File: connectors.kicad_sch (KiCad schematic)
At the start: 12 parts, among them J1101 VN_1611_Interface, J1102 AMPSEAL_35, J1103 Banana_Jack, J1104 Banana_Jack

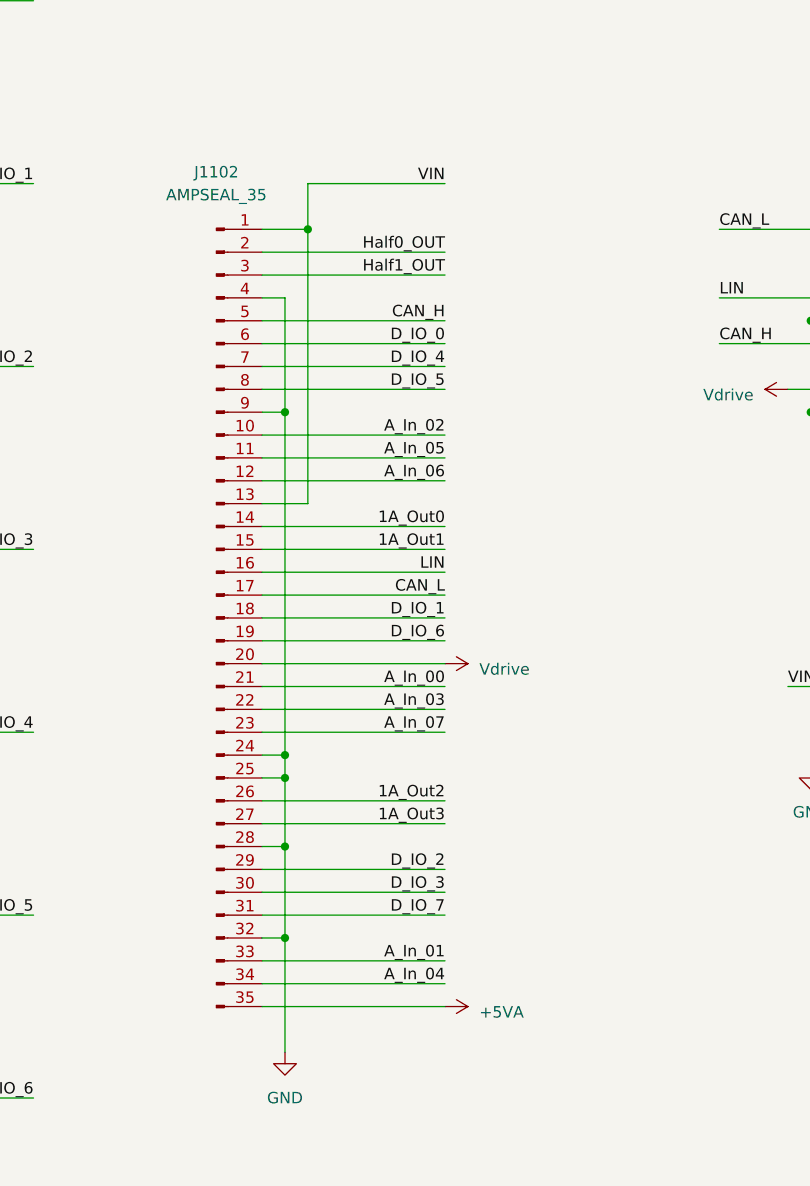
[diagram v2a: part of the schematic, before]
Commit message: placed components and began routing
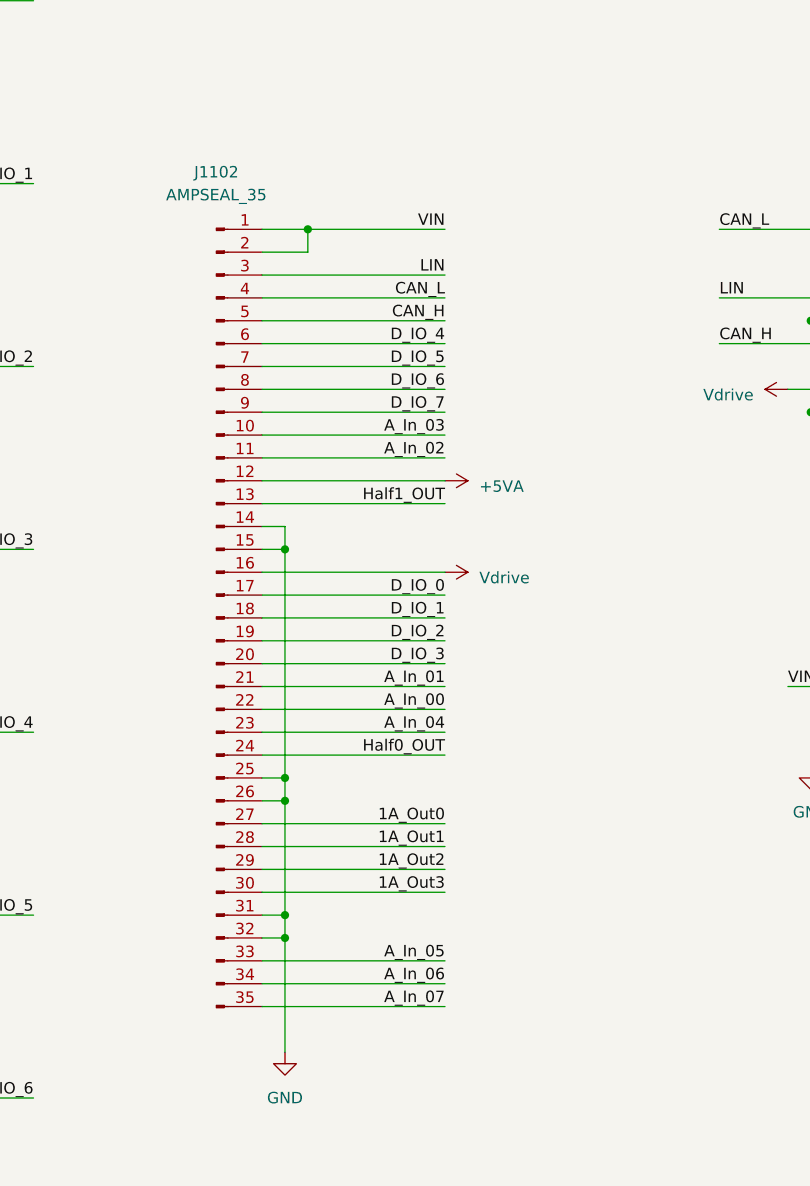
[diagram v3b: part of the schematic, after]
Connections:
- net +5VA: now also J1102.12 (Pin_12); no longer J1102.35 (Pin_35)
- net 1A_Out0: now also J1102.27 (Pin_27); no longer J1102.14 (Pin_14)
- net 1A_Out1: now also J1102.28 (Pin_28); no longer J1102.15 (Pin_15)
- net 1A_Out2: now also J1102.29 (Pin_29); no longer J1102.26 (Pin_26)
- net 1A_Out3: now also J1102.30 (Pin_30); no longer J1102.27 (Pin_27)
- net A_In_00: now also J1102.22 (Pin_22); no longer J1102.21 (Pin_21)
- net A_In_01: now also J1102.21 (Pin_21); no longer J1102.33 (Pin_33)
- net A_In_02: now also J1102.11 (Pin_11); no longer J1102.10 (Pin_10)
- net A_In_03: now also J1102.10 (Pin_10); no longer J1102.22 (Pin_22)
- net A_In_04: now also J1102.23 (Pin_23); no longer J1102.34 (Pin_34)
- net A_In_05: now also J1102.33 (Pin_33); no longer J1102.11 (Pin_11)
- net A_In_06: now also J1102.34 (Pin_34); no longer J1102.12 (Pin_12)
- net A_In_07: now also J1102.35 (Pin_35); no longer J1102.23 (Pin_23)
- net CAN_L: now also J1102.4 (Pin_4); no longer J1102.17 (Pin_17)
- net D_IO_0: now also J1102.17 (Pin_17); no longer J1102.6 (Pin_6)
- net D_IO_2: now also J1102.19 (Pin_19); no longer J1102.29 (Pin_29)
- net D_IO_3: now also J1102.20 (Pin_20); no longer J1102.30 (Pin_30)
- net D_IO_4: now also J1102.6 (Pin_6); no longer J1102.7 (Pin_7)
- net D_IO_5: now also J1102.7 (Pin_7); no longer J1102.8 (Pin_8)
- net D_IO_6: now also J1102.8 (Pin_8); no longer J1102.19 (Pin_19)
- net D_IO_7: now also J1102.9 (Pin_9); no longer J1102.31 (Pin_31)
- net GND: now also J1102.14 (Pin_14), J1102.15 (Pin_15), J1102.26 (Pin_26), J1102.31 (Pin_31); no longer J1102.24 (Pin_24), J1102.28 (Pin_28), J1102.4 (Pin_4), J1102.9 (Pin_9)
- net Half0_OUT: now also J1102.24 (Pin_24); no longer J1102.2 (Pin_2)
- net Half1_OUT: now also J1102.13 (Pin_13); no longer J1102.3 (Pin_3)
- net LIN: now also J1102.3 (Pin_3); no longer J1102.16 (Pin_16)
- net VIN: now also J1102.2 (Pin_2); no longer J1102.13 (Pin_13)
- net Vdrive: now also J1102.16 (Pin_16); no longer J1102.20 (Pin_20)

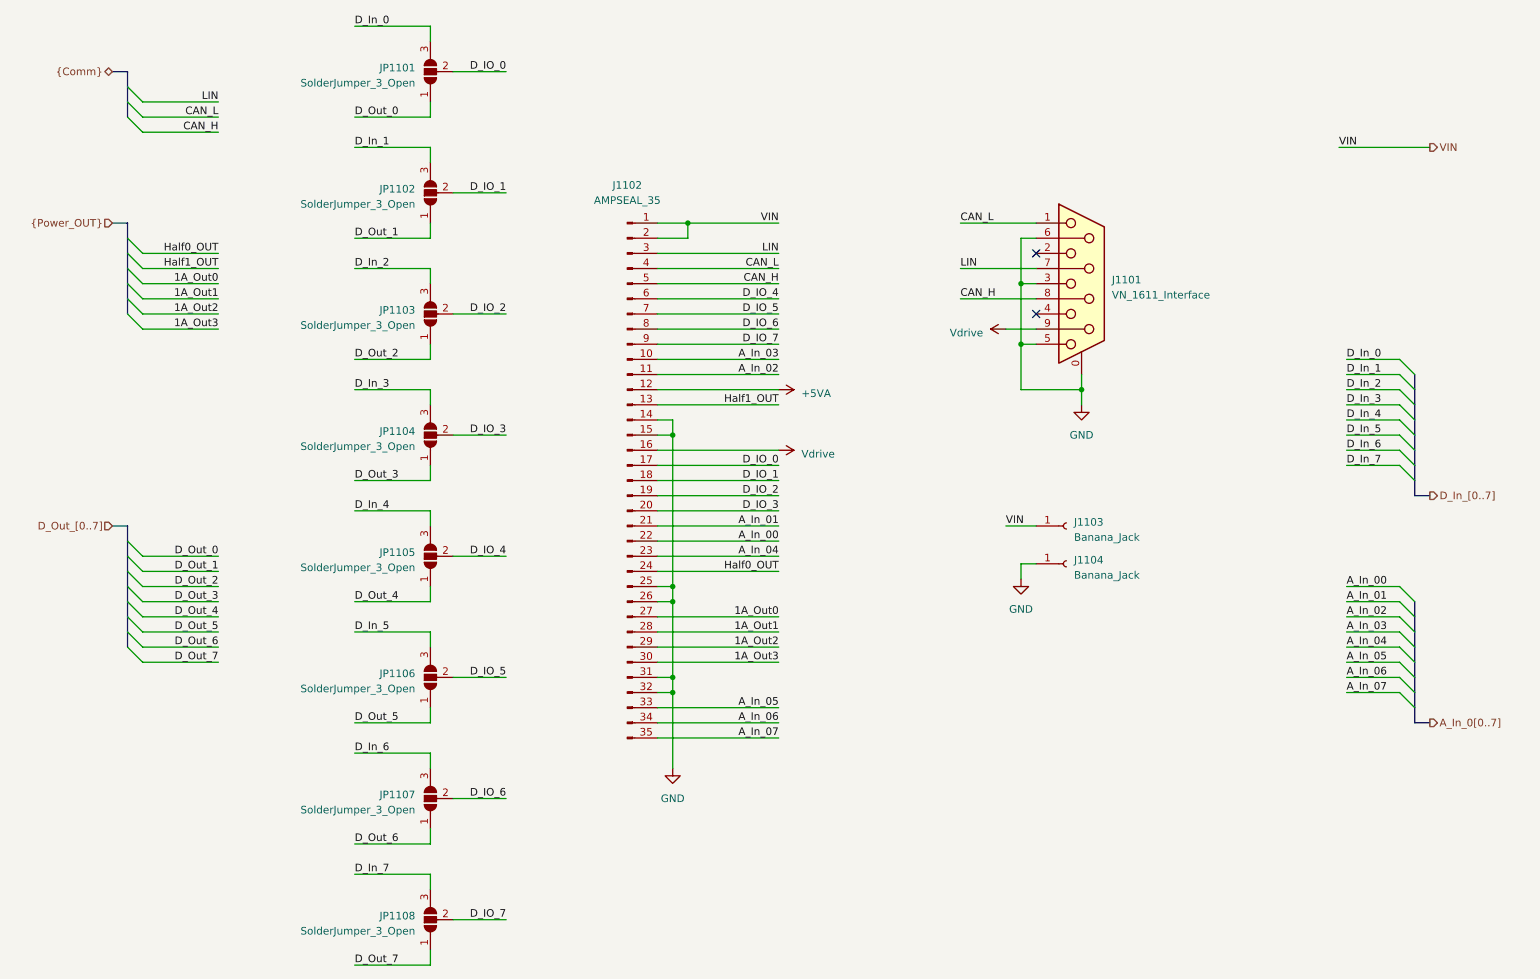
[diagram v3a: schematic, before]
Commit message: hierarchical sheets for digital I/O and replaced power supply jumpers with relays
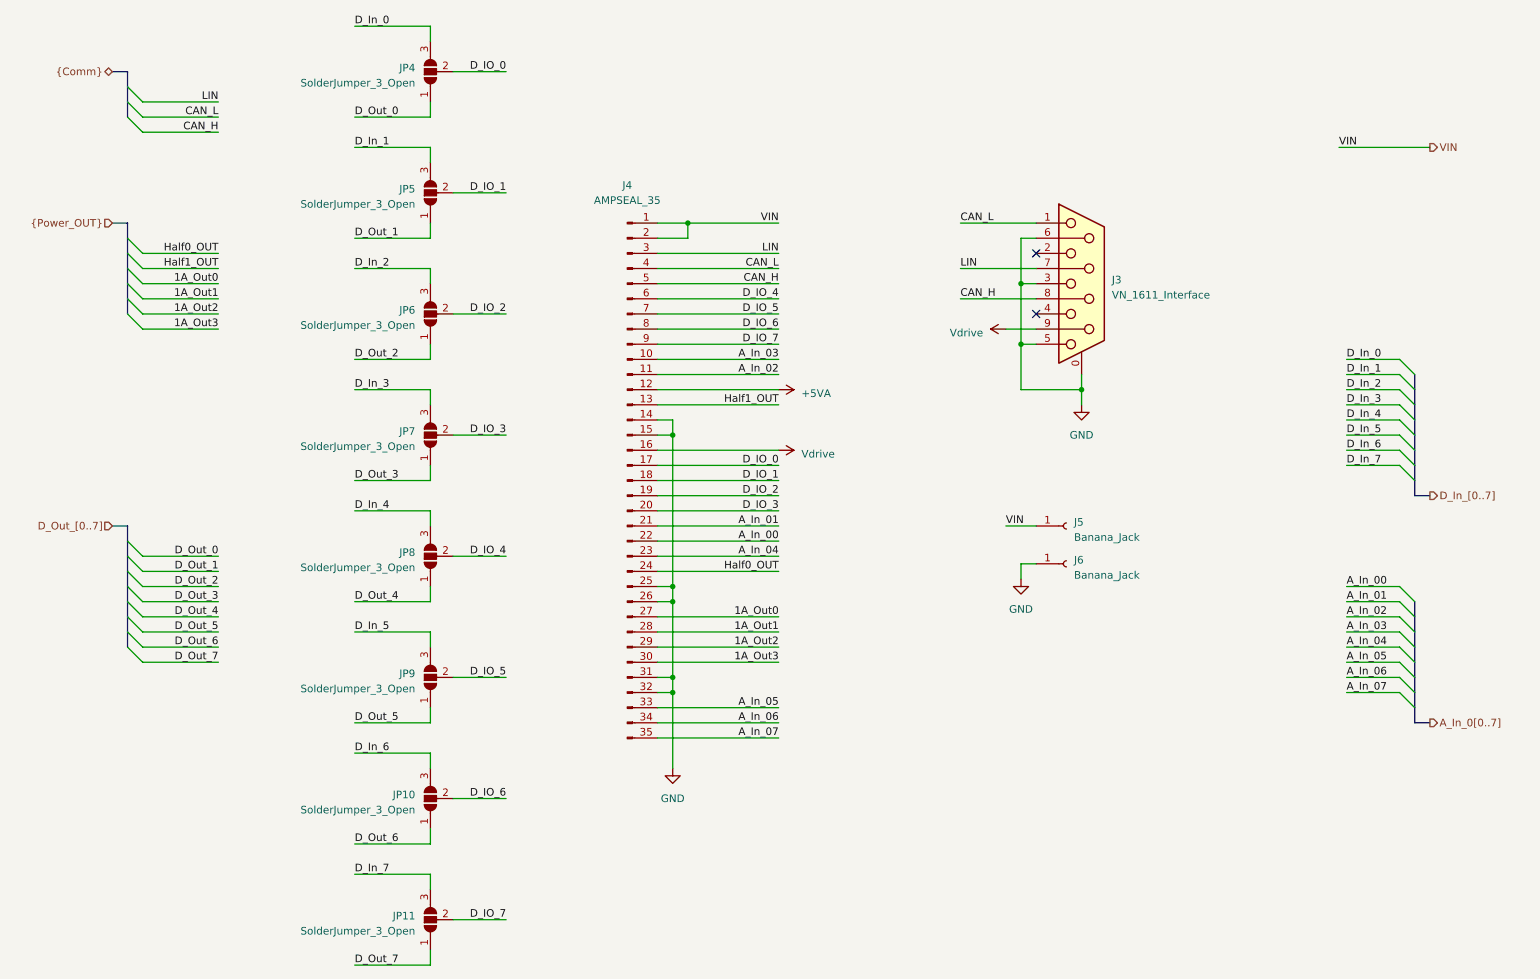
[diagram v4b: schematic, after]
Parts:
- renumbered J1101 to J3, J1102 to J4, J1103 to J5, J1104 to J6, JP1107 to JP10, JP1108 to JP11, JP1101 to JP4, JP1102 to JP5, JP1103 to JP6, JP1104 to JP7, JP1105 to JP8, JP1106 to JP9
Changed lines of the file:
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@@
   (symbol (lib_id "Jumper:SolderJumper_3_Open") (at 88.9 127 90) (unit 1)
     (in_bom yes) (on_board yes) (dnp no) (fields_autoplaced)
-    (property "Reference" "JP1106" (at 86.36 126.365 90)
+    (property "Reference" "JP9" (at 86.36 126.365 90)
       (effects (font (size 1.27 1.27)) (justify left))
     )
@@
       (project "Sensor_Board"
         (path "/e2a0eb17-0eae-4cdd-befd-118f8728b921/276bb215-b19a-4afa-b073-6f1d222ea979"
-          (reference "JP1106") (unit 1)
+          (reference "JP9") (unit 1)
         )
       )
@@
   (symbol (lib_id "power:Vdrive") (at 147.32 88.9 270) (unit 1)
     (in_bom yes) (on_board yes) (dnp no) (fields_autoplaced)
-    (property "Reference" "#PWR01103" (at 143.51 83.82 0)
+    (property "Reference" "#PWR0148" (at 143.51 83.82 0)
       (effects (font (size 1.27 1.27)) hide)
     )
@@
       (project "Sensor_Board"
         (path "/e2a0eb17-0eae-4cdd-befd-118f8728b921/276bb215-b19a-4afa-b073-6f1d222ea979"
-          (reference "#PWR01103") (unit 1)
+          (reference "#PWR0148") (unit 1)
         )
       )
@@
   (symbol (lib_id "power:GND") (at 198.12 81.28 0) (unit 1)
     (in_bom yes) (on_board yes) (dnp no) (fields_autoplaced)
-    (property "Reference" "#PWR01102" (at 198.12 87.63 0)
+    (property "Reference" "#PWR0147" (at 198.12 87.63 0)
       (effects (font (size 1.27 1.27)) hide)
     )
@@
       (project "Sensor_Board"
         (path "/e2a0eb17-0eae-4cdd-befd-118f8728b921/276bb215-b19a-4afa-b073-6f1d222ea979"
-          (reference "#PWR01102") (unit 1)
+          (reference "#PWR0147") (unit 1)
         )
       )
@@
   (symbol (lib_id "Connector:DE9_Receptacle_MountingHoles") (at 198.12 60.96 0) (unit 1)
     (in_bom yes) (on_board yes) (dnp no) (fields_autoplaced)
-    (property "Reference" "J1101" (at 203.2 60.325 0)
+    (property "Reference" "J3" (at 203.2 60.325 0)
       (effects (font (size 1.27 1.27)) (justify left))
     )
@@
       (project "Sensor_Board"
         (path "/e2a0eb17-0eae-4cdd-befd-118f8728b921/276bb215-b19a-4afa-b073-6f1d222ea979"
-          (reference "J1101") (unit 1)
+          (reference "J3") (unit 1)
         )
       )
@@
   (symbol (lib_id "Connector:Conn_01x01_Socket") (at 195.58 101.6 0) (unit 1)
     (in_bom yes) (on_board yes) (dnp no) (fields_autoplaced)
-    (property "Reference" "J1103" (at 196.85 100.965 0)
+    (property "Reference" "J5" (at 196.85 100.965 0)
       (effects (font (size 1.27 1.27)) (justify left))
     )
@@
       (project "Sensor_Board"
         (path "/e2a0eb17-0eae-4cdd-befd-118f8728b921/276bb215-b19a-4afa-b073-6f1d222ea979"
-          (reference "J1103") (unit 1)
+          (reference "J5") (unit 1)
         )
       )
@@
   (symbol (lib_id "Jumper:SolderJumper_3_Open") (at 88.9 25.4 90) (unit 1)
     (in_bom yes) (on_board yes) (dnp no) (fields_autoplaced)
-    (property "Reference" "JP1101" (at 86.36 24.765 90)
+    (property "Reference" "JP4" (at 86.36 24.765 90)
       (effects (font (size 1.27 1.27)) (justify left))
     )
@@
       (project "Sensor_Board"
         (path "/e2a0eb17-0eae-4cdd-befd-118f8728b921/276bb215-b19a-4afa-b073-6f1d222ea979"
-          (reference "JP1101") (unit 1)
+          (reference "JP4") (unit 1)
         )
       )
@@
   (symbol (lib_id "power:GND") (at 187.96 110.49 0) (unit 1)
     (in_bom yes) (on_board yes) (dnp no) (fields_autoplaced)
-    (property "Reference" "#PWR01104" (at 187.96 116.84 0)
+    (property "Reference" "#PWR0149" (at 187.96 116.84 0)
       (effects (font (size 1.27 1.27)) hide)
     )
@@
       (project "Sensor_Board"
         (path "/e2a0eb17-0eae-4cdd-befd-118f8728b921/276bb215-b19a-4afa-b073-6f1d222ea979"
-          (reference "#PWR01104") (unit 1)
+          (reference "#PWR0149") (unit 1)
         )
       )
@@
   (symbol (lib_id "Jumper:SolderJumper_3_Open") (at 88.9 106.68 90) (unit 1)
     (in_bom yes) (on_board yes) (dnp no) (fields_autoplaced)
-    (property "Reference" "JP1105" (at 86.36 106.045 90)
+    (property "Reference" "JP8" (at 86.36 106.045 90)
       (effects (font (size 1.27 1.27)) (justify left))
     )
@@
       (project "Sensor_Board"
         (path "/e2a0eb17-0eae-4cdd-befd-118f8728b921/276bb215-b19a-4afa-b073-6f1d222ea979"
-          (reference "JP1105") (unit 1)
+          (reference "JP8") (unit 1)
         )
       )
@@
   (symbol (lib_id "Jumper:SolderJumper_3_Open") (at 88.9 147.32 90) (unit 1)
     (in_bom yes) (on_board yes) (dnp no) (fields_autoplaced)
-    (property "Reference" "JP1107" (at 86.36 146.685 90)
+    (property "Reference" "JP10" (at 86.36 146.685 90)
       (effects (font (size 1.27 1.27)) (justify left))
     )
@@
       (project "Sensor_Board"
         (path "/e2a0eb17-0eae-4cdd-befd-118f8728b921/276bb215-b19a-4afa-b073-6f1d222ea979"
-          (reference "JP1107") (unit 1)
+          (reference "JP10") (unit 1)
         )
       )
@@
   (symbol (lib_id "Connector:Conn_01x01_Socket") (at 195.58 107.95 0) (unit 1)
     (in_bom yes) (on_board yes) (dnp no) (fields_autoplaced)
-    (property "Reference" "J1104" (at 196.85 107.315 0)
+    (property "Reference" "J6" (at 196.85 107.315 0)
       (effects (font (size 1.27 1.27)) (justify left))
     )
@@
       (project "Sensor_Board"
         (path "/e2a0eb17-0eae-4cdd-befd-118f8728b921/276bb215-b19a-4afa-b073-6f1d222ea979"
-          (reference "J1104") (unit 1)
+          (reference "J6") (unit 1)
         )
       )
@@
   (symbol (lib_id "power:GND") (at 129.54 142.24 0) (unit 1)
     (in_bom yes) (on_board yes) (dnp no) (fields_autoplaced)
-    (property "Reference" "#PWR01106" (at 129.54 148.59 0)
+    (property "Reference" "#PWR0150" (at 129.54 148.59 0)
       (effects (font (size 1.27 1.27)) hide)
     )
@@
       (project "Sensor_Board"
         (path "/e2a0eb17-0eae-4cdd-befd-118f8728b921/276bb215-b19a-4afa-b073-6f1d222ea979"
-          (reference "#PWR01106") (unit 1)
+          (reference "#PWR0150") (unit 1)
         )
       )
@@
   (symbol (lib_id "Jumper:SolderJumper_3_Open") (at 88.9 86.36 90) (unit 1)
     (in_bom yes) (on_board yes) (dnp no) (fields_autoplaced)
-    (property "Reference" "JP1104" (at 86.36 85.725 90)
+    (property "Reference" "JP7" (at 86.36 85.725 90)
       (effects (font (size 1.27 1.27)) (justify left))
     )
@@
       (project "Sensor_Board"
         (path "/e2a0eb17-0eae-4cdd-befd-118f8728b921/276bb215-b19a-4afa-b073-6f1d222ea979"
-          (reference "JP1104") (unit 1)
+          (reference "JP7") (unit 1)
         )
       )
@@
   (symbol (lib_id "Jumper:SolderJumper_3_Open") (at 88.9 66.04 90) (unit 1)
     (in_bom yes) (on_board yes) (dnp no) (fields_autoplaced)
-    (property "Reference" "JP1103" (at 86.36 65.405 90)
+    (property "Reference" "JP6" (at 86.36 65.405 90)
       (effects (font (size 1.27 1.27)) (justify left))
     )
@@
       (project "Sensor_Board"
         (path "/e2a0eb17-0eae-4cdd-befd-118f8728b921/276bb215-b19a-4afa-b073-6f1d222ea979"
-          (reference "JP1103") (unit 1)
+          (reference "JP6") (unit 1)
         )
       )
@@
   (symbol (lib_id "power:+5VA") (at 147.32 78.74 270) (unit 1)
     (in_bom yes) (on_board yes) (dnp no) (fields_autoplaced)
-    (property "Reference" "#PWR01105" (at 143.51 78.74 0)
+    (property "Reference" "#PWR0146" (at 143.51 78.74 0)
       (effects (font (size 1.27 1.27)) hide)
     )
@@
       (project "Sensor_Board"
         (path "/e2a0eb17-0eae-4cdd-befd-118f8728b921/276bb215-b19a-4afa-b073-6f1d222ea979"
-          (reference "#PWR01105") (unit 1)
+          (reference "#PWR0146") (unit 1)
         )
       )
@@
   (symbol (lib_id "Jumper:SolderJumper_3_Open") (at 88.9 45.72 90) (unit 1)
     (in_bom yes) (on_board yes) (dnp no) (fields_autoplaced)
-    (property "Reference" "JP1102" (at 86.36 45.085 90)
+    (property "Reference" "JP5" (at 86.36 45.085 90)
       (effects (font (size 1.27 1.27)) (justify left))
     )
@@
       (project "Sensor_Board"
         (path "/e2a0eb17-0eae-4cdd-befd-118f8728b921/276bb215-b19a-4afa-b073-6f1d222ea979"
-          (reference "JP1102") (unit 1)
+          (reference "JP5") (unit 1)
         )
       )
@@
         )
         (path "/e2a0eb17-0eae-4cdd-befd-118f8728b921/276bb215-b19a-4afa-b073-6f1d222ea979"
-          (reference "#PWR01101") (unit 1)
+          (reference "#PWR0145") (unit 1)
         )
       )
@@
   (symbol (lib_id "FaSTTUBe_connectors:AMPSEAL_35_90deg") (at 121.92 93.98 0) (unit 1)
     (in_bom yes) (on_board yes) (dnp no)
-    (property "Reference" "J1102" (at 121.92 44.45 0)
+    (property "Reference" "J4" (at 121.92 44.45 0)
       (effects (font (size 1.27 1.27)))
     )
@@
       (project "Sensor_Board"
         (path "/e2a0eb17-0eae-4cdd-befd-118f8728b921/276bb215-b19a-4afa-b073-6f1d222ea979"
-          (reference "J1102") (unit 1)
+          (reference "J4") (unit 1)
         )
       )
@@
   (symbol (lib_id "Jumper:SolderJumper_3_Open") (at 88.9 167.64 90) (unit 1)
     (in_bom yes) (on_board yes) (dnp no) (fields_autoplaced)
-    (property "Reference" "JP1108" (at 86.36 167.005 90)
+    (property "Reference" "JP11" (at 86.36 167.005 90)
       (effects (font (size 1.27 1.27)) (justify left))
     )
@@
       (project "Sensor_Board"
         (path "/e2a0eb17-0eae-4cdd-befd-118f8728b921/276bb215-b19a-4afa-b073-6f1d222ea979"
-          (reference "JP1108") (unit 1)
-        )
-      )
+          (reference "JP11") (unit 1)
+        )
+      )
